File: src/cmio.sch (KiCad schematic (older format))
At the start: 32 parts, among them J1 USB_POWER, J10 Micro_SD_Card_TFP09_2_12B, J2 TEST_3V3, J3 TEST_2V8, J4 TEST_GND, J5 BANK0, J6 USB_OTG, J7 CM3Lite, J8 TVOUT, J9 BANK1, SW1 Reset, U1 LD3985M18R, U2 LD3985M28R, U3 ISL91107IR

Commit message: Complete Redesign
- Fixed the net name of OTGID.
- Fixed USB OTG power switch.
- Added more decoupling capacitors.
- Connected VBAT directly to 5V.
- Changed Buck-Boost converter to Buck converter with reduced output
current.

Signed-off-by: Mahyar Koshkouei <mk@deltabeard.com>
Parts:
- removed C10, C9: 22uF, Capacitors_SMD:C_1206_HandSoldering, symbol C_Small
- removed C5: 1uF, Capacitors_SMD:C_1206_HandSoldering, symbol C_Small
- removed J2: TEST_3V3, Measurement_Points:Measurement_Point_Round-SMD-Pad_Small, symbol TEST_1P
- removed J3: TEST_2V8, Measurement_Points:Measurement_Point_Round-SMD-Pad_Small, symbol TEST_1P
- removed J4: TEST_GND, Measurement_Points:Measurement_Point_Round-TH_Small, symbol TEST_1P
- removed JP1: 3.3 OUT, Pin_Headers:Pin_Header_Straight_2x01_Pitch2.54mm_SMD, symbol Jumper_NO_Small
- removed JP2: PWRUSB, Pin_Headers:Pin_Header_Straight_2x01_Pitch2.54mm_SMD, symbol Jumper_NC_Small
- removed L1: 1uH, Inductors:Inductor_Taiyo-Yuden_NR-40xx_HandSoldering, symbol L_Core_Ferrite_Small
- removed U3: ISL91107IR, foot:20_TQFP, symbol ISL91107IR
- added C1, C12: 10uF, Capacitors_SMD:C_1206_HandSoldering, symbol C_Small
- added C10, C15, C19: 120uF, Capacitors_SMD:CP_Elec_6.3x5.8, symbol CP1_Small
- added C11, C14, C17: 0.1uF, Capacitors_SMD:C_0805_HandSoldering, symbol C_Small
- added C13, C16: 100pF, Capacitors_SMD:C_0805_HandSoldering, symbol C_Small
- added C4: 1uF, Capacitors_SMD:C_1206_HandSoldering, symbol C_Small
- added L1: 3.3uH, foot:Inductor_1008, symbol L_Small
- added R1: 100, Resistors_SMD:R_0805_HandSoldering, symbol R_Small
- added R2: 82K, Resistors_SMD:R_0805_HandSoldering, symbol R_Small
- added R3: 10K, Resistors_SMD:R_0805_HandSoldering, symbol R_Small
- added R4: 680K, Resistors_SMD:R_0805_HandSoldering, symbol R_Small
- added U3: AP6015, Housings_SSOP:MSOP-10_3x3mm_Pitch0.5mm, symbol AP6015
- added U4: AP2401, Housings_SSOP:MSOP-8_3x3mm_Pitch0.65mm, symbol AP2401
- C18: renamed from C11; value 4.7uF -> 10uF
- C5: renamed from C3; footprint Capacitors_SMD:C_1206_HandSoldering -> Capacitors_SMD:C_0805_HandSoldering
- C6: renamed from C4; footprint Capacitors_SMD:C_1206_HandSoldering -> Capacitors_SMD:C_0805_HandSoldering
- C7: value 22uF -> 100pF; footprint Capacitors_SMD:C_1206_HandSoldering -> Capacitors_SMD:C_0805_HandSoldering
- renumbered C1 to C2, C2 to C3, C6 to C8, C8 to C9, J5 to J2, J6 to J3, J7 to J4, J8 to J5, J9 to J6, J10 to J7, R1 to R5, R2 to R6, R3 to R7, R4 to R8
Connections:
- net labels added: +3.3V, OTGID
- net labels removed: OTDIG
- wire segments 161 -> 167
- no-connect marks 67 -> 68
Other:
- note added: "Filtering"

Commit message: Finish PCB Routing
Signed-off-by: Mahyar Koshkouei <mk@deltabeard.com>
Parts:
- removed C19: 120uF, Capacitors_SMD:CP_Elec_6.3x5.8, symbol CP1_Small
- C1, C12, C18, C2, C3, C4, C8, C9: footprint Capacitors_SMD:C_1206_HandSoldering -> Capacitors_SMD:C_0805_HandSoldering
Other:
- note added: "Micro SD Card Decoupling"
- note removed: "Filtering"
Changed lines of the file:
@@
 F 0 "C2" H 1610 6870 50  0000 L CNN
 F 1 "1uF" H 1610 6720 50  0000 L CNN
-F 2 "Capacitors_SMD:C_1206_HandSoldering" H 1600 6800 50  0001 C CNN
+F 2 "Capacitors_SMD:C_0805_HandSoldering" H 1600 6800 50  0001 C CNN
 F 3 "" H 1600 6800 50  0001 C CNN
 	1    1600 6800
@@
 F 0 "C8" H 3010 6820 50  0000 L CNN
 F 1 "1uF" H 3010 6670 50  0000 L CNN
-F 2 "Capacitors_SMD:C_1206_HandSoldering" H 3000 6750 50  0001 C CNN
+F 2 "Capacitors_SMD:C_0805_HandSoldering" H 3000 6750 50  0001 C CNN
 F 3 "" H 3000 6750 50  0001 C CNN
 	1    3000 6750
@@
 F 0 "C3" H 1660 8120 50  0000 L CNN
 F 1 "1uF" H 1660 7970 50  0000 L CNN
-F 2 "Capacitors_SMD:C_1206_HandSoldering" H 1650 8050 50  0001 C CNN
+F 2 "Capacitors_SMD:C_0805_HandSoldering" H 1650 8050 50  0001 C CNN
 F 3 "" H 1650 8050 50  0001 C CNN
 	1    1650 8050
@@
 F 0 "C9" H 3060 8070 50  0000 L CNN
 F 1 "1uF" H 3060 7920 50  0000 L CNN
-F 2 "Capacitors_SMD:C_1206_HandSoldering" H 3050 8000 50  0001 C CNN
+F 2 "Capacitors_SMD:C_0805_HandSoldering" H 3050 8000 50  0001 C CNN
 F 3 "" H 3050 8000 50  0001 C CNN
 	1    3050 8000
@@
 F 0 "C18" H 14542 846 50  0000 L CNN
 F 1 "10uF" H 14542 755 50  0000 L CNN
-F 2 "Capacitors_SMD:C_1206_HandSoldering" H 14450 800 50  0001 C CNN
+F 2 "Capacitors_SMD:C_0805_HandSoldering" H 14450 800 50  0001 C CNN
 F 3 "" H 14450 800 50  0001 C CNN
 	1    14450 800
@@
 F 0 "C1" H 1460 9370 50  0000 L CNN
 F 1 "10uF" H 1460 9220 50  0000 L CNN
-F 2 "Capacitors_SMD:C_1206_HandSoldering" H 1450 9300 50  0001 C CNN
+F 2 "Capacitors_SMD:C_0805_HandSoldering" H 1450 9300 50  0001 C CNN
 F 3 "" H 1450 9300 50  0001 C CNN
 	1    1450 9300
@@
 F 0 "C4" H 1710 9720 50  0000 L CNN
 F 1 "1uF" H 1710 9570 50  0000 L CNN
-F 2 "Capacitors_SMD:C_1206_HandSoldering" H 1700 9650 50  0001 C CNN
+F 2 "Capacitors_SMD:C_0805_HandSoldering" H 1700 9650 50  0001 C CNN
 F 3 "" H 1700 9650 50  0001 C CNN
 	1    1700 9650
@@
 F 0 "C12" H 3560 9420 50  0000 L CNN
 F 1 "10uF" H 3560 9270 50  0000 L CNN
-F 2 "Capacitors_SMD:C_1206_HandSoldering" H 3550 9350 50  0001 C CNN
+F 2 "Capacitors_SMD:C_0805_HandSoldering" H 3550 9350 50  0001 C CNN
 F 3 "" H 3550 9350 50  0001 C CNN
 	1    3550 9350
@@
 	3350 5650 3350 5550
 $Comp
-L CP1_Small C19
-U 1 1 59AD629D
-P 14900 800
-F 0 "C19" H 14910 870 50  0000 L CNN
-F 1 "120uF" H 15000 750 50  0000 L CNN
-F 2 "Capacitors_SMD:CP_Elec_6.3x5.8" H 14900 800 50  0001 C CNN
-F 3 "" H 14900 800 50  0001 C CNN
-	1    14900 800
-	1    0    0    -1
-$EndComp
-$Comp
 L C_Small C17
 U 1 1 59AD6A7A
@@
 	1    0    0    -1
 $EndComp
-Wire Wire Line
-	13650 700  14900 700
 Connection ~ 14450 700
-Wire Wire Line
-	13650 900  14900 900
 Connection ~ 14450 900
 $Comp
@@
 Connection ~ 14050 900
 Text Notes 14000 600  0    60   ~ 0
-Filtering
+Micro SD Card Decoupling
 $Comp
 L C_Small C13
@@
 	3900 9250 3900 9050
 Connection ~ 3900 9050
+Wire Wire Line
+	13650 700  14450 700
+Wire Wire Line
+	14450 900  13650 900
 $EndSCHEMATC

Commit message: Simplify CM3 Module Part
Additionally removed some unnecessary decoupling capacitors.
Additionally changes the pin allocations on GPIO Bank 1 to optimise
track length.
Additionally added PWR_FLAG to fix some ERC errors.

Signed-off-by: Mahyar Koshkouei <mk@deltabeard.com>
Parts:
- removed C10: 120uF, Capacitors_SMD:CP_Elec_6.3x5.8, symbol CP1_Small
- removed C13, C16: 100pF, Capacitors_SMD:C_0805_HandSoldering, symbol C_Small
- removed C18: 10uF, Capacitors_SMD:C_0805_HandSoldering, symbol C_Small
- added C11: 220uF, Capacitors_SMD:CP_Elec_6.3x5.8, symbol CP1_Small
- C14: renamed from C15; value 120uF -> 220uF
- renumbered C12 to C10, C11 to C12, C14 to C13, C17 to C15, R4 to R3, R3 to R4
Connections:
- wire segments 167 -> 164
- no-connect marks 68 -> 59
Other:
- moved on the sheet: C1, C10, C12, C13, C14, C15, C2, C3, C4, C5, C6, C7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

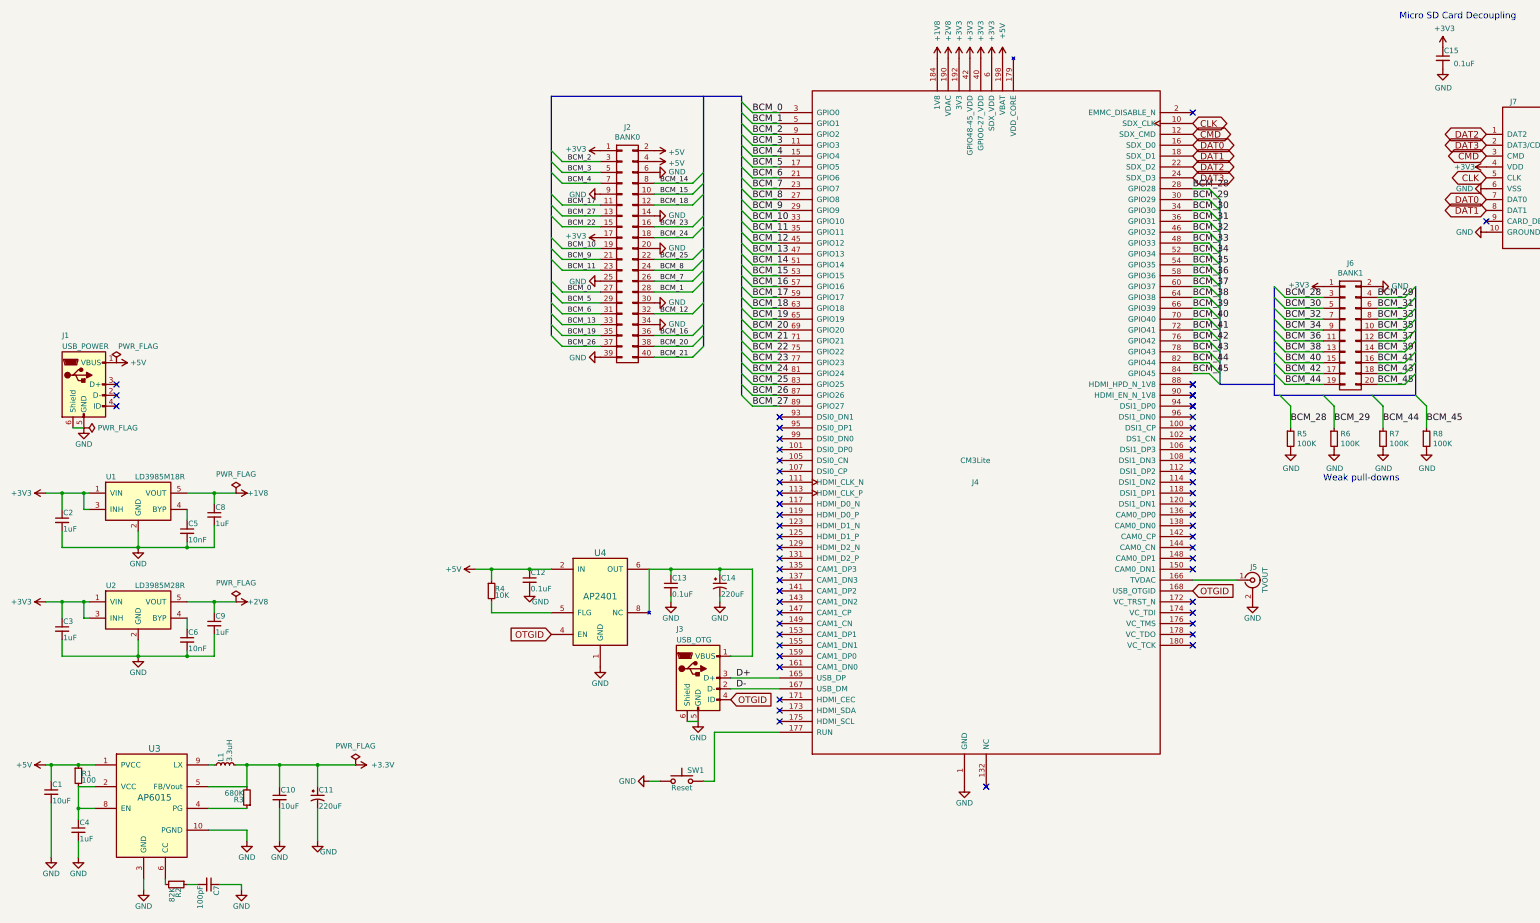
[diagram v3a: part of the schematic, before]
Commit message: Improve CM3 Footprint
Additionally removed electrolytic capacitors.
Re-annotated components and cleared board.

Signed-off-by: Mahyar Koshkouei <mk@deltabeard.com>
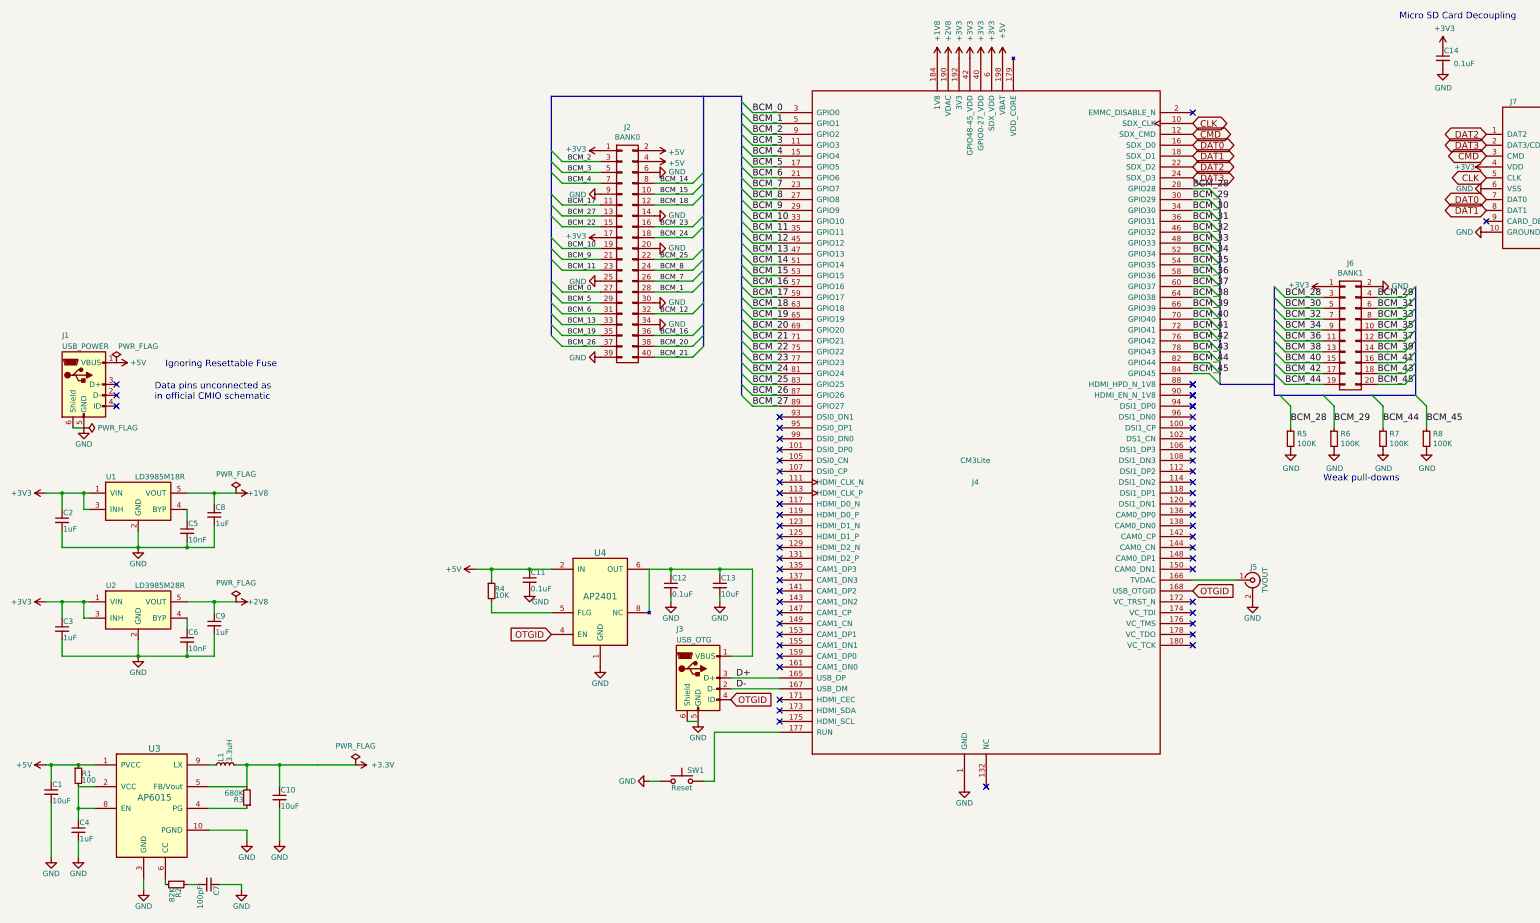
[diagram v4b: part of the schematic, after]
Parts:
- removed C11, C14: 220uF, Capacitors_SMD:CP_Elec_6.3x5.8, symbol CP1_Small
- added C13: 10uF, Capacitors_SMD:C_0805_HandSoldering, symbol C_Small
- renumbered C12 to C11, C13 to C12, C15 to C14
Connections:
- net GND: now also C13.2
- net at C12.1, J3.1 (VBUS), U4.6 (OUT)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: now also C13.1
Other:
- note added: "Data pins unconnected as\nin official CMIO schematic"
- note added: "Ignoring Resettable Fuse"

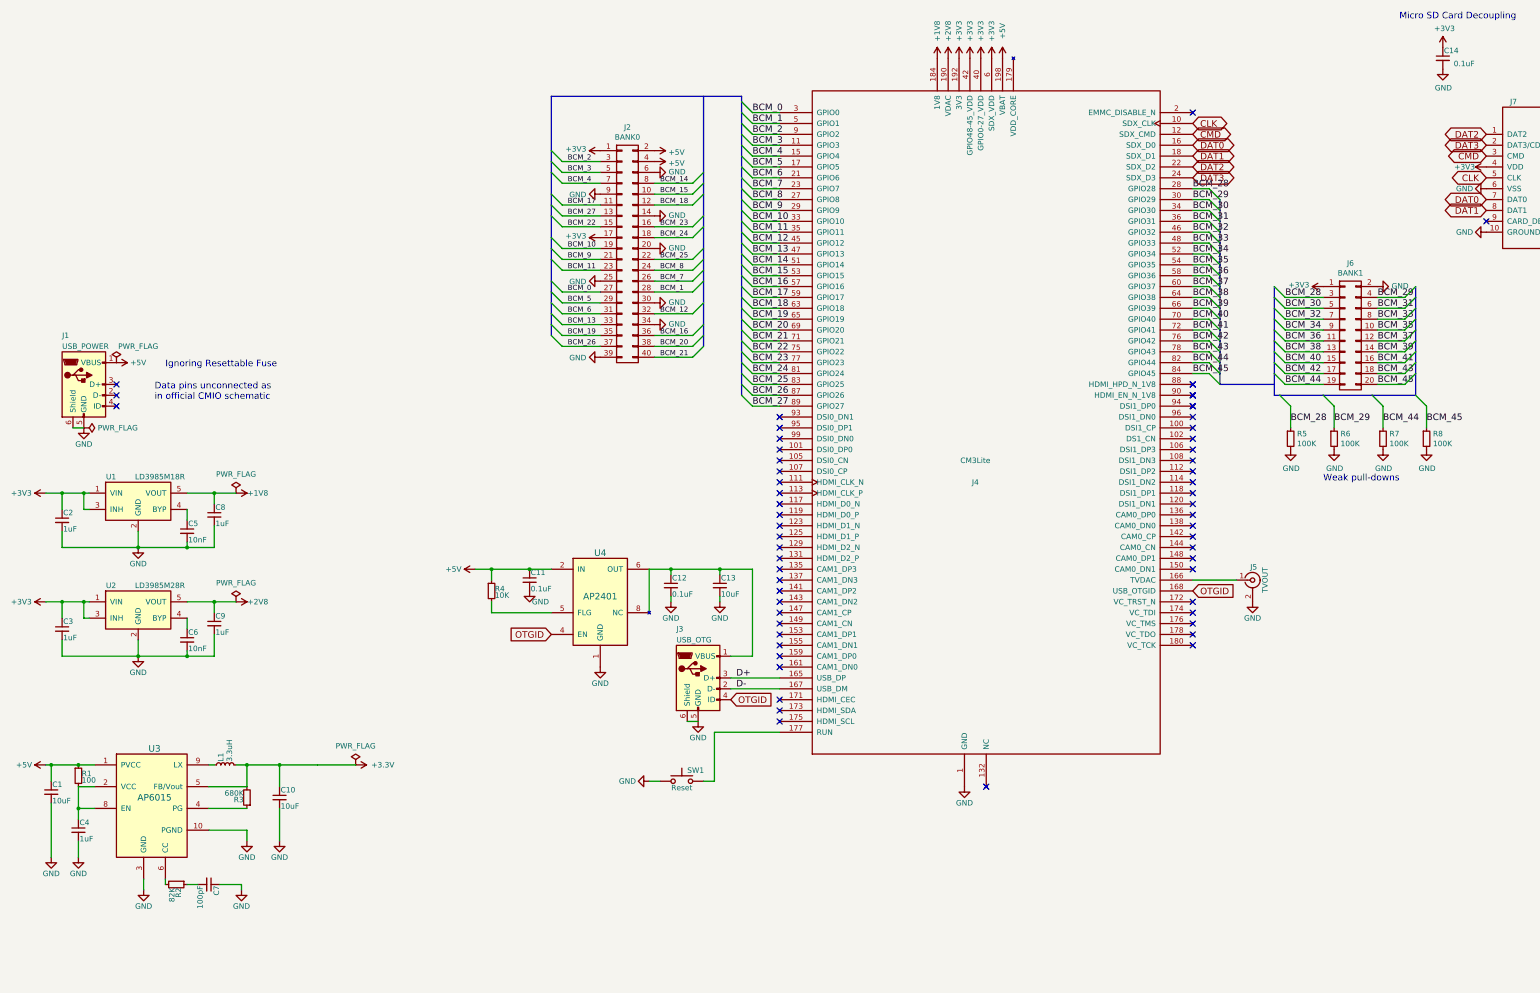
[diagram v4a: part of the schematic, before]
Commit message: Replaced ICs
Using buck converters with simpler design requirements and lower cost.
Using an LDO for VDAC due to lower noise and low current requirements.

Signed-off-by: Mahyar Koshkouei <mahyar.koshkouei@gmail.com>
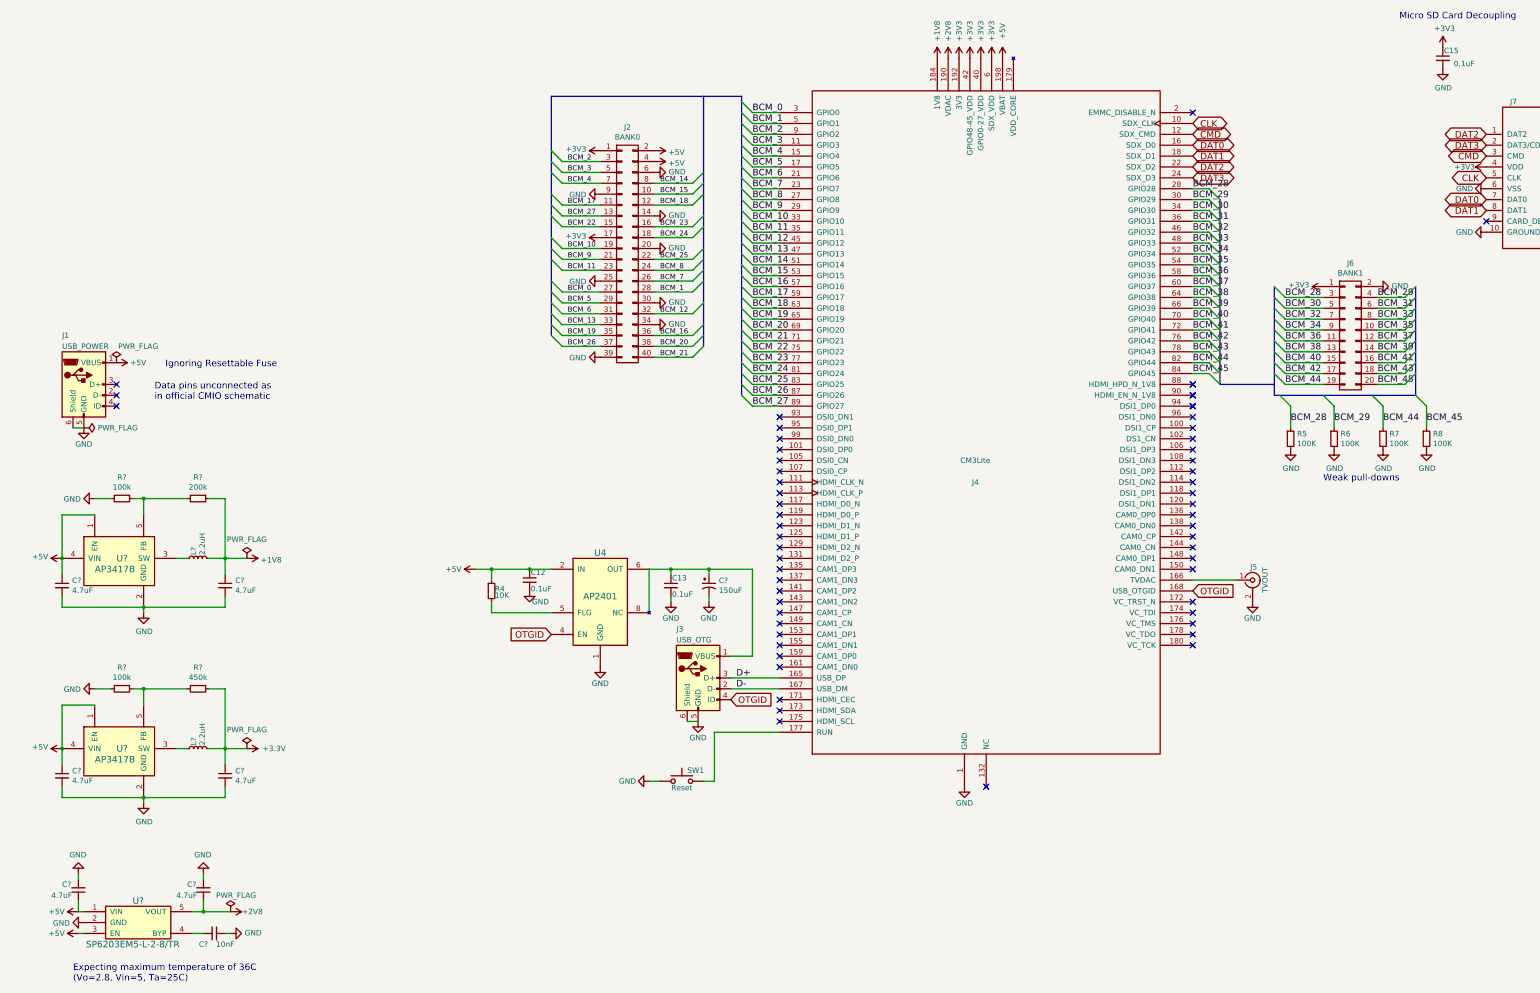
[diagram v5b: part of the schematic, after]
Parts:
- removed C1, C10, C13: 10uF, Capacitors_SMD:C_0805_HandSoldering, symbol C_Small
- removed C2, C3, C4, C8, C9: 1uF, Capacitors_SMD:C_0805_HandSoldering, symbol C_Small
- removed C5, C6: 10nF, Capacitors_SMD:C_0805_HandSoldering, symbol C_Small
- removed C7: 100pF, Capacitors_SMD:C_0805_HandSoldering, symbol C_Small
- removed L1: 3.3uH, foot:Inductor_1008, symbol L_Small
- removed R1: 100, Resistors_SMD:R_0805_HandSoldering, symbol R_Small
- removed R2: 82K, Resistors_SMD:R_0805_HandSoldering, symbol R_Small
- removed R3: 680K, Resistors_SMD:R_0805_HandSoldering, symbol R_Small
- removed U1: LD3985M18R, TO_SOT_Packages_SMD:SOT-23-5, symbol LD3985M18R
- removed U2: LD3985M28R, TO_SOT_Packages_SMD:SOT-23-5, symbol LD3985M28R
- removed U3: AP6015, Housings_SSOP:MSOP-10_3x3mm_Pitch0.5mm, symbol AP6015
- added C?: 10nF, symbol C_Small
- added C? (x6): 4.7uF, symbol C_Small
- added C?: 150uF, symbol CP1_Small
- added L? (x2): 2.2uH, foot:Inductor_1008, symbol L_Small
- added R?: 450k, symbol R_Small
- added R? (x2): 100k, symbol R_Small
- added R?: 200k, symbol R_Small
- added U?: SP6203EM5-L-2-8/TR, symbol SP6203
- added U? (x2): AP3417B, symbol AP3417B
- J2: footprint Pin_Headers:Pin_Header_Straight_2x20_Pitch2.54mm_SMD -> Pin_Headers:Pin_Header_Straight_2x20_Pitch2.54mm
- J4: footprint foot:Socket_SODIMM_DDR1-2_TE_1612618 -> foot:CM3_Socket_SODIMM_DDR1-2_TE_1612618
- J6: footprint Pin_Headers:Pin_Header_Straight_2x10_Pitch2.54mm_SMD -> Pin_Headers:Pin_Header_Straight_2x10_Pitch2.54mm
- renumbered C11 to C12, C12 to C13, C14 to C15
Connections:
- net +1V8: now also C?.1, L?.2, R?.1
- net +2V8: now also C?.1, U?.5 (VOUT)
- net +3V3: now also C?.1, L?.2, R?.1
- net +5V: now also C?.1, C?.1, C?.1, U?.1 (EN), U?.1 (EN), U?.1 (VIN), U?.3 (EN), U?.4 (VIN), U?.4 (VIN)
- net GND: now also C?.1, C?.2, C?.2, C?.2, C?.2, C?.2, C?.2, C?.2, R?.2, R?.2, U?.2 (GND), U?.2 (GND), U?.2 (GND)
- net at C13.1, J3.1 (VBUS), U4.6 (OUT)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: now also C?.1
- new net: C?.2, U?.4 (BYP)
- new net: L?.1, U?.3 (SW) (x2)
- new net: R?.1, R?.2, U?.5 (FB) (x2)
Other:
- note added: "Expecting maximum temperature of 36C\n(Vo=2.8, Vin=5, Ta=25C)"

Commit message: Add associations
Signed-off-by: Mahyar Koshkouei <mahyar.koshkouei@gmail.com>
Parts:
- C1, C2, C3, C4, C5, C6, C7: renamed from C?; footprint (none) -> Capacitors_SMD:C_0805_HandSoldering
- C10: renamed from C?; footprint (none) -> Capacitors_SMD:CP_Elec_6.3x7.7
- L1, L2: renamed from L?; footprint foot:Inductor_1008 -> Inductors_NEOSID:Neosid_Inductor_SM-NE29_SMD1008
- R1, R2, R3, R4: renamed from R?; footprint (none) -> Resistors_SMD:R_0805_HandSoldering
- U1, U2, U3: renamed from U?; footprint (none) -> TO_SOT_Packages_SMD:SOT-23-5_HandSoldering
- renumbered C15 to C11, C12 to C8, C13 to C9, R4 to R5, R5 to R6, R6 to R7, R7 to R8, R8 to R9
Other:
- moved on the sheet: C10, C11, C8, C9, J2, J3, J4, J5, J6, J7, R5, R6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
